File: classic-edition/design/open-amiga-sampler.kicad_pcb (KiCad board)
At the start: 2 copper layers, 37 x 34 mm, 19 parts, among them J1 Left, J2 Right, J3 DB25_Male, U1 ADC0820CCN, U2 MCP6002-xP

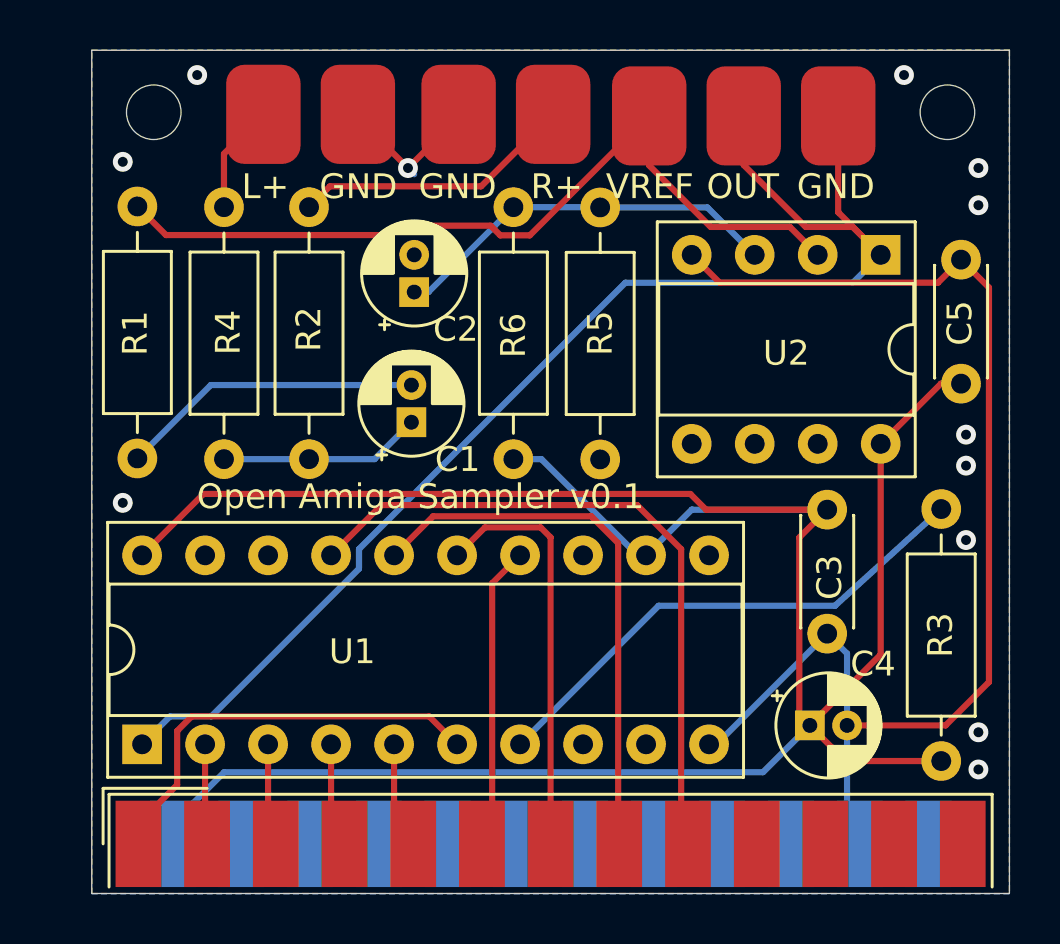
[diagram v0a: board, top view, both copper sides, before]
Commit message: Updated silk screen text
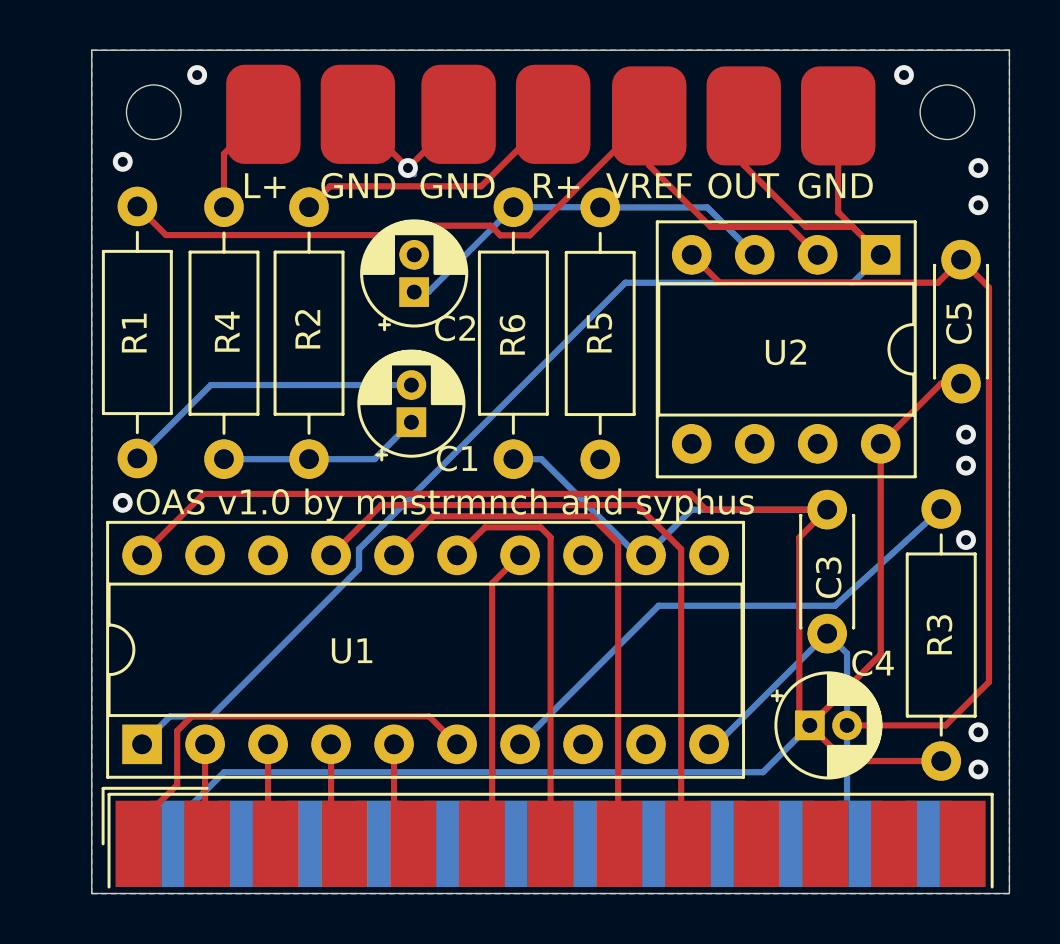
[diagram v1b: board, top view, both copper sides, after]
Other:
- board text added: "OAS v1.0 by mnstrmnch and syphus"
- board text removed: "Open Amiga Sampler v0.1"
